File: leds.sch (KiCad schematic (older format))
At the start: 61 parts

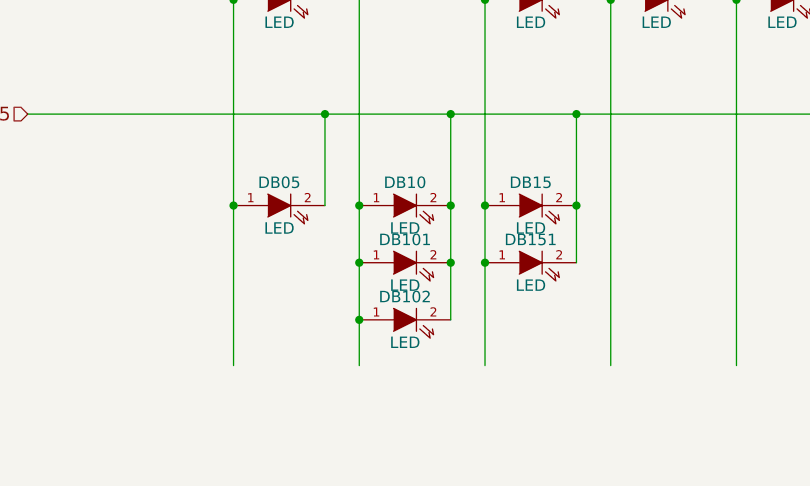
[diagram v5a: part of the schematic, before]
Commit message: Remove unnecessary related SWs to S10
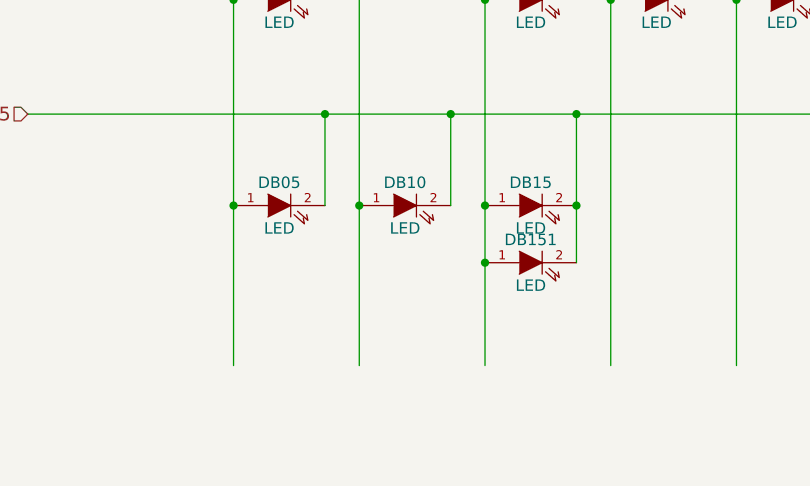
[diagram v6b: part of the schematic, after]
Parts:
- removed DB101, DB102: LED, symbol device:LED
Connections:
- wire segments 194 -> 190
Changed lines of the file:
@@
-$EndComp
-$Comp
-L device:LED DB101
-U 1 1 51C065B4
-P 2800 5800
-F 0 "DB101" H 2800 5900 50  0000 C CNN
-F 1 "LED" H 2800 5700 50  0000 C CNN
-F 2 "" H 2800 5800 60  0001 C CNN
-F 3 "" H 2800 5800 60  0001 C CNN
-	1    2800 5800
-	1    0    0    -1
-$EndComp
-$Comp
-L device:LED DB102
-U 1 1 51C065BA
-P 2800 6050
-F 0 "DB102" H 2800 6150 50  0000 C CNN
-F 1 "LED" H 2800 5950 50  0000 C CNN
-F 2 "" H 2800 6050 60  0001 C CNN
-F 3 "" H 2800 6050 60  0001 C CNN
-	1    2800 6050
-	1    0    0    -1
 $EndComp
 $Comp
@@
 Connection ~ 4800 5800
 Connection ~ 4800 6050
-Connection ~ 3000 5550
-Connection ~ 3000 5800
-Connection ~ 2600 5800
-Connection ~ 2600 6050
 Connection ~ 3150 5800
 Connection ~ 3550 5550
@@
 	2450 5150 3000 5150
 Wire Wire Line
-	2600 5550 2600 5800
-Wire Wire Line
 	3000 5150 3550 5150
 Wire Wire Line
@@
 	4800 6050 4800 6250
 Wire Wire Line
-	3000 5550 3000 5800
-Wire Wire Line
-	3000 5800 3000 6050
-Wire Wire Line
-	2600 5800 2600 6050
-Wire Wire Line
-	2600 6050 2600 6250
-Wire Wire Line
 	3150 5800 3150 6250
 Wire Wire Line
@@
 Wire Wire Line
 	2050 5550 2050 6250
+Wire Wire Line
+	2600 5550 2600 6250
 $EndSCHEMATC

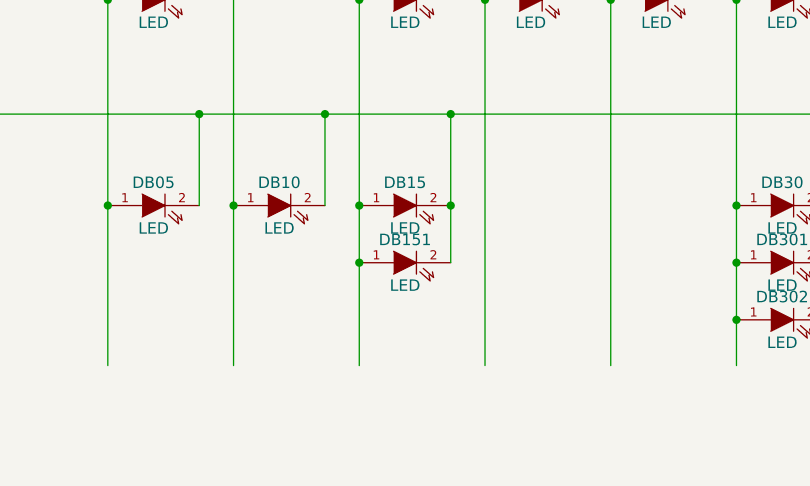
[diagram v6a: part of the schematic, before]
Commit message: Remove unnecessary related SW to SW15
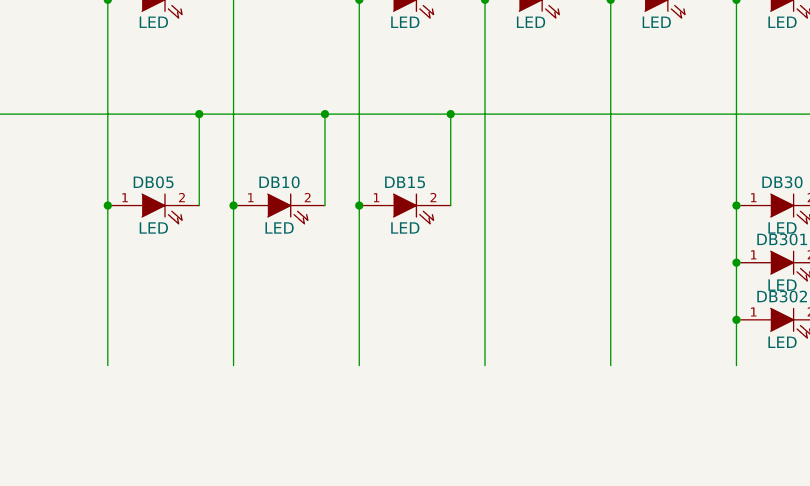
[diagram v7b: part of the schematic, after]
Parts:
- removed DB151: LED, symbol device:LED
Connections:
- wire segments 190 -> 188
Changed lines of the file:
@@
-	1    0    0    -1
-$EndComp
-$Comp
-L device:LED DB151
-U 1 1 51C06955
-P 3350 5800
-F 0 "DB151" H 3350 5900 50  0000 C CNN
-F 1 "LED" H 3350 5700 50  0000 C CNN
-F 2 "" H 3350 5800 60  0001 C CNN
-F 3 "" H 3350 5800 60  0001 C CNN
-	1    3350 5800
 	1    0    0    -1
 $EndComp
@@
 Connection ~ 4800 5800
 Connection ~ 4800 6050
-Connection ~ 3150 5800
-Connection ~ 3550 5550
 Text Notes 3250 2800 0    60   ~ 0
 wasd\ncluster
@@
 	3000 5150 3550 5150
 Wire Wire Line
-	3150 5550 3150 5800
-Wire Wire Line
 	3550 5150 5200 5150
 Wire Wire Line
@@
 	4800 6050 4800 6250
 Wire Wire Line
-	3150 5800 3150 6250
-Wire Wire Line
-	3550 5550 3550 5800
-Wire Wire Line
 	9200 4650 9200 6250
 Wire Wire Line
@@
 Wire Wire Line
 	2600 5550 2600 6250
+Wire Wire Line
+	3150 5550 3150 6250
 $EndSCHEMATC

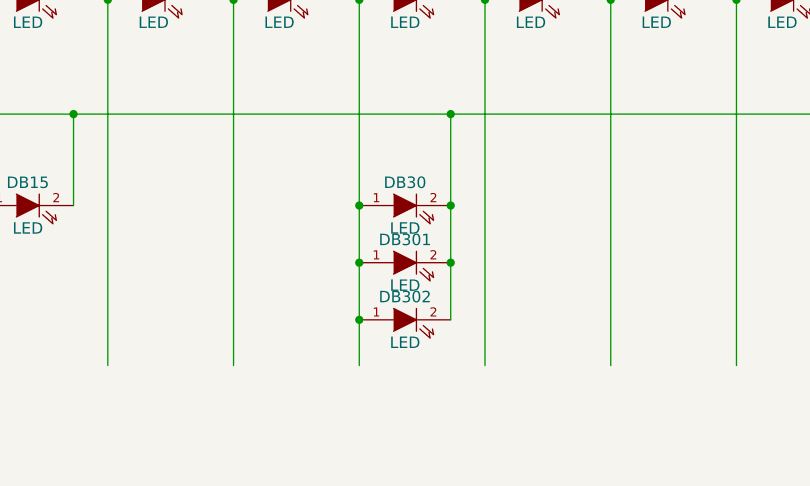
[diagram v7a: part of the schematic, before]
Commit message: Remove unnecessary related SWs to SW30
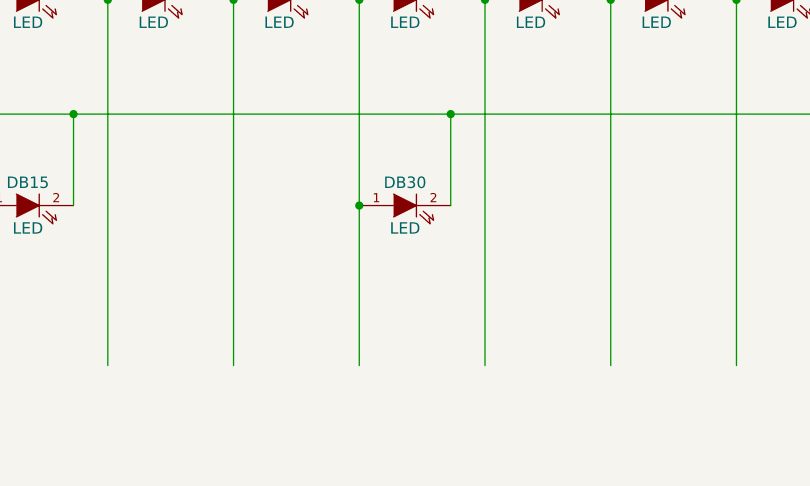
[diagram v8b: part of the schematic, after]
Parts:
- removed DB301, DB302: LED, mx1a:MX1A-led_no3d, symbol device:LED
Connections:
- wire segments 188 -> 184
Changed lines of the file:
@@
-	1    0    0    -1
-$EndComp
-$Comp
-L device:LED DB301
-U 1 1 51C0300D
-P 5000 5800
-F 0 "DB301" H 5000 5900 50  0000 C CNN
-F 1 "LED" H 5000 5700 50  0000 C CNN
-F 2 "mx1a:MX1A-led_no3d" H 5000 5800 60  0001 C CNN
-F 3 "" H 5000 5800 60  0001 C CNN
-	1    5000 5800
-	1    0    0    -1
-$EndComp
-$Comp
-L device:LED DB302
-U 1 1 51C03013
-P 5000 6050
-F 0 "DB302" H 5000 6150 50  0000 C CNN
-F 1 "LED" H 5000 5950 50  0000 C CNN
-F 2 "mx1a:MX1A-led_no3d" H 5000 6050 60  0001 C CNN
-F 3 "" H 5000 6050 60  0001 C CNN
-	1    5000 6050
 	1    0    0    -1
 $EndComp
@@
 Connection ~ 7950 5550
 Connection ~ 7550 5800
-Connection ~ 5200 5550
-Connection ~ 5200 5800
-Connection ~ 4800 5800
-Connection ~ 4800 6050
 Text Notes 3250 2800 0    60   ~ 0
 wasd\ncluster
@@
 	7950 5150 9900 5150
 Wire Wire Line
-	4800 5550 4800 5800
-Wire Wire Line
 	7950 5550 7950 5800
 Wire Wire Line
 	7550 5800 7550 6250
 Wire Wire Line
-	5200 5550 5200 5800
-Wire Wire Line
-	5200 5800 5200 6050
-Wire Wire Line
-	4800 5800 4800 6050
-Wire Wire Line
-	4800 6050 4800 6250
-Wire Wire Line
 	9200 4650 9200 6250
 Wire Wire Line
@@
 Wire Wire Line
 	3150 5550 3150 6250
+Wire Wire Line
+	4800 5550 4800 6250
 $EndSCHEMATC
